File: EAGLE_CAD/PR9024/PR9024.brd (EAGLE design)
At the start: 70 x 70 mm, 75 parts, among them SW1 C&K_PTS645

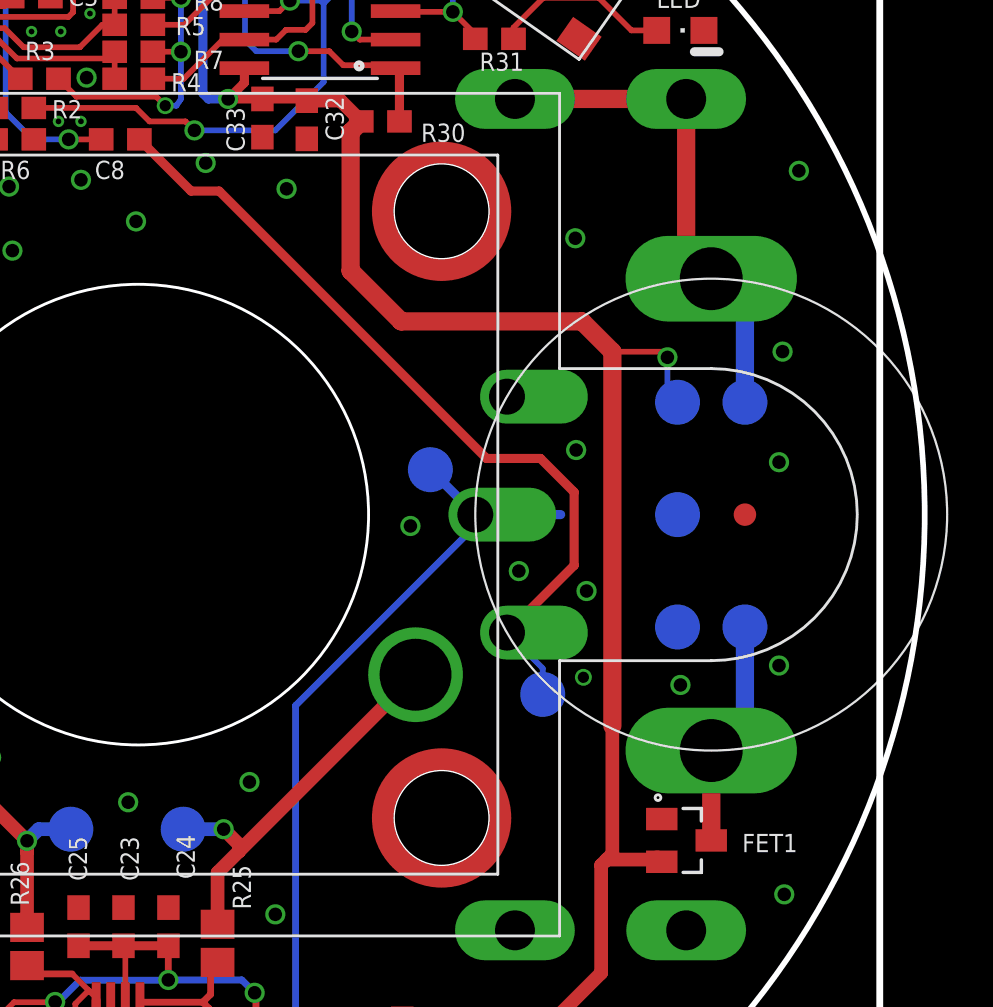
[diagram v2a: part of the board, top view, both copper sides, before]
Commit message: updated pot & rerouted stuff
new pot is Hong Yu Innovation Electronics Co
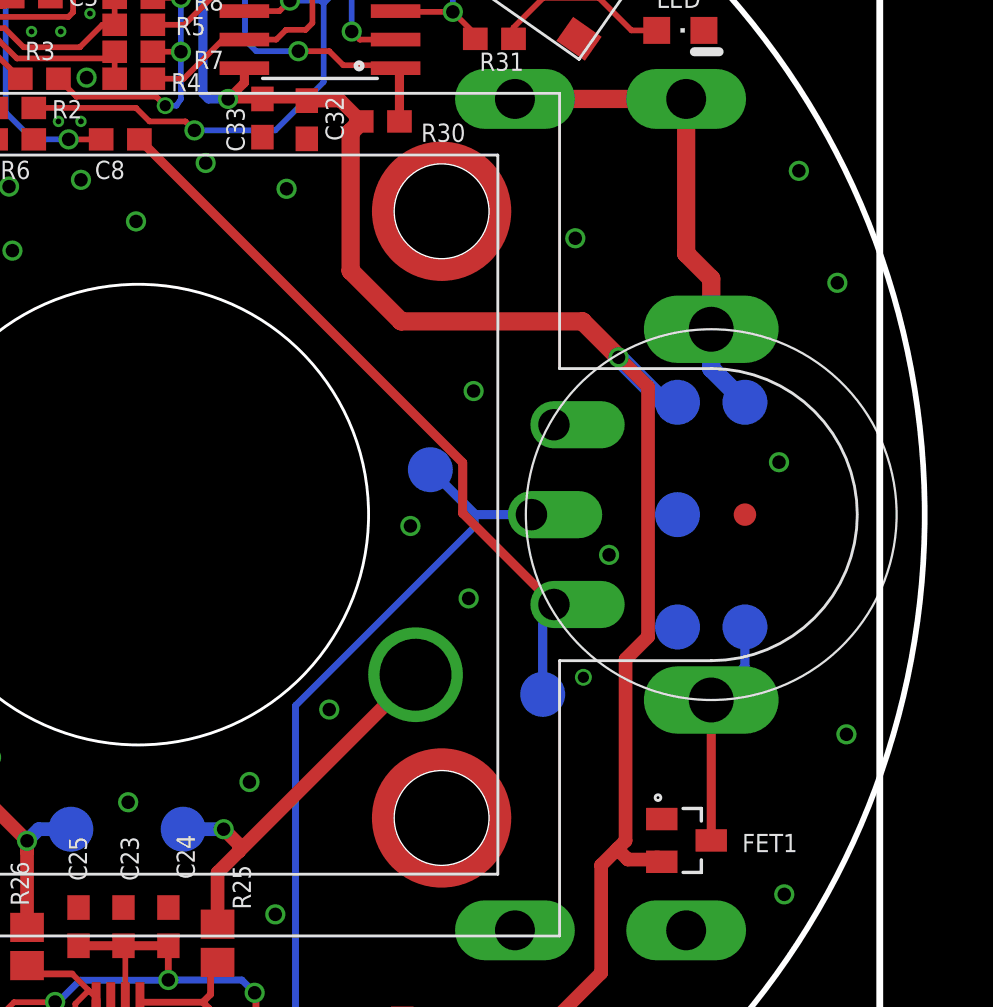
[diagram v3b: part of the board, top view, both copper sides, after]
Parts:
- R1: value (none) -> VOLUME_POT; device PR_Parts_Library:RV170SF_SW_POT -> PR_Parts_Library:H17112NS_A10K_L20F-002
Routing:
- net A_IN: track 36.8 -> 32.5 mm
- net A_OUT: track 35.7 -> 34.4 mm
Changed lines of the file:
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@@
 <?xml version="1.0" encoding="utf-8"?>
 <!DOCTYPE eagle SYSTEM "eagle.dtd">
-<eagle version="6.6.0">
+<eagle version="7.7.0">
 <drawing>
 <settings>
@@
 <rectangle x1="35.7111" y1="10.3543" x2="35.7873" y2="10.3797" layer="26" rot="R90"/>
 <rectangle x1="35.6857" y1="10.2781" x2="35.8635" y2="10.3035" layer="26" rot="R90"/>
-<text x="64" y="35" size="0.8128" layer="26" font="vector" ratio="22" rot="MR270" align="center">PR9024
+<text x="65.25" y="35" size="0.8128" layer="26" font="vector" ratio="22" rot="MR270" align="center">PR9024
 Born + tuned in Brooklyn
 http://thepublicrad.io</text>
@@
 <pass name="Default">
 <param name="RoutingGrid" value="50mil"/>
+<param name="AutoGrid" value="1"/>
+<param name="Efforts" value="0"/>
+<param name="TopRouterVariant" value="1"/>
 <param name="tpViaShape" value="round"/>
 <param name="PrefDir.1" value="|"/>
@@
 </element>
 <element name="ANT_MOUNT" library="PR_Parts_Library" package="PEM_M3" value="DNP" x="9.5" y="35" locked="yes" smashed="yes"/>
-<element name="R1" library="PR_Parts_Library" package="RV170SF_SW_POT" value="" x="60.5" y="35" locked="yes" rot="R270">
-<attribute name="MFG_PN" value="RV170SF-43-20F-A10K - supplied by CL Labs" x="60.5" y="35" size="1.778" layer="27" rot="R270" display="off"/>
-</element>
+<element name="R1" library="PR_Parts_Library" package="H17112NS_A10K_L20F-002" value="VOLUME_POT" x="60.5" y="35" locked="yes" rot="R270"/>
 <element name="MCU" library="PR_Parts_Library" package="8-SOIC" value="" x="43.075" y="56.775" smashed="yes" rot="R90">
 <attribute name="NAME" x="41.473" y="59.475" size="0.8128" layer="25" font="vector" ratio="16"/>
@@
 <via x="21.8" y="13.9" extent="1-16" drill="0.6"/>
 <via x="39.95" y="23.1" extent="1-16" drill="0.6"/>
-<via x="51.9375" y="32.4875" extent="1-16" drill="0.6"/>
 <via x="21.15375" y="64.95375" extent="1-16" drill="0.6"/>
 <contactref element="SW1" pad="P$1"/>
@@
 <via x="41.1" y="17.21" extent="1-16" drill="0.6"/>
 <via x="47.1125" y="34.495" extent="1-16" drill="0.6"/>
-<via x="54.4875" y="37.875" extent="1-16" drill="0.6"/>
-<via x="54.95" y="31.6" extent="1-16" drill="0.6"/>
+<via x="49.925" y="40.5" extent="1-16" drill="0.6"/>
 <via x="54.45" y="47.3" extent="1-16" drill="0.6"/>
 <via x="30.25" y="56.5" extent="1-16" drill="0.254"/>
@@
 <via x="33.36" y="59.265" extent="1-16" drill="0.5"/>
 <via x="54.81" y="27.76" extent="1-16" drill="0.5"/>
-<via x="59.13" y="27.42" extent="1-16" drill="0.6"/>
 <contactref element="LED" pad="C"/>
 <via x="44.2175" y="6.60875" extent="1-16" drill="0.6"/>
@@
 <via x="5.8675" y="51.235" extent="1-16" drill="0.6"/>
 <via x="23.7125" y="7.325" extent="1-16" drill="0.6"/>
-<via x="63.675" y="42.255" extent="1-16" drill="0.6"/>
-<via x="63.51625" y="28.285" extent="1-16" drill="0.6"/>
+<via x="66.1125" y="45.3175" extent="1-16" drill="0.6"/>
+<via x="66.51625" y="25.2225" extent="1-16" drill="0.6"/>
 <via x="63.51625" y="37.33375" extent="1-16" drill="0.6"/>
 <via x="51.59125" y="6.7675" extent="1-16" drill="0.6"/>
@@
 <vertex x="2" y="2"/>
 </polygon>
+<via x="55.95375" y="33.20875" extent="1-16" drill="0.6"/>
+<via x="49.70375" y="31.27125" extent="1-16" drill="0.6"/>
+<via x="43.5" y="26.325" extent="1-16" drill="0.6"/>
 </signal>
 <signal name="N$1">
@@
 <contactref element="T5" pad="TP"/>
 <contactref element="C32" pad="1"/>
-<wire x1="56.1" y1="25.6" x2="56.1" y2="42.25" width="0.8128" layer="1"/>
 <contactref element="FET1" pad="2"/>
 <wire x1="58.1" y1="19.65" x2="58.3" y2="19.55" width="0.8128" layer="1"/>
 <wire x1="55.6" y1="14.6" x2="55.6" y2="19.4" width="0.6096" layer="1"/>
-<wire x1="58.1" y1="19.65" x2="55.85" y2="19.65" width="0.6096" layer="1"/>
-<wire x1="55.85" y1="19.65" x2="55.6" y2="19.4" width="0.6096" layer="1"/>
-<wire x1="55.85" y1="19.65" x2="56.1" y2="19.9" width="0.6096" layer="1"/>
-<wire x1="56.1" y1="19.9" x2="56.1" y2="25.6" width="0.6096" layer="1"/>
-<wire x1="56.1" y1="42.25" x2="54.75" y2="43.6" width="0.8128" layer="1"/>
-<wire x1="54.75" y1="43.6" x2="46.7" y2="43.6" width="0.8128" layer="1"/>
+<wire x1="54.775" y1="43.6" x2="46.7" y2="43.6" width="0.8128" layer="1"/>
 <wire x1="46.7" y1="43.6" x2="44.45" y2="45.85" width="0.8128" layer="1"/>
-<wire x1="59" y1="40" x2="58.55" y2="40.45" width="0.254" layer="16"/>
-<wire x1="58.55" y1="40.45" x2="58.55" y2="42" width="0.254" layer="16"/>
-<via x="58.55" y="42" extent="1-16" drill="0.6"/>
-<wire x1="58.55" y1="42" x2="58.3" y2="42.25" width="0.254" layer="1"/>
-<wire x1="58.3" y1="42.25" x2="56.1" y2="42.25" width="0.254" layer="1"/>
 <wire x1="41.9375" y1="12.13" x2="46.43" y2="12.13" width="0.3048" layer="1"/>
 <wire x1="46.43" y1="12.13" x2="46.75" y2="11.81" width="0.3048" layer="1"/>
@@
 <wire x1="33.625" y1="62.125" x2="34.675" y2="62.125" width="0.254" layer="1"/>
 <wire x1="34.675" y1="62.125" x2="34.7" y2="62.15" width="0.254" layer="1"/>
+<wire x1="59" y1="40" x2="58.375" y2="40" width="0.8128" layer="16"/>
+<wire x1="58.375" y1="40" x2="56.375" y2="42" width="0.8128" layer="16"/>
+<via x="56.375" y="42" extent="1-16" drill="0.6"/>
+<wire x1="56.375" y1="42" x2="54.775" y2="43.6" width="0.8128" layer="1"/>
+<wire x1="55.6" y1="19.4" x2="56.31875" y2="20.11875" width="0.6096" layer="1"/>
+<wire x1="56.31875" y1="20.11875" x2="56.6875" y2="20.4875" width="0.6096" layer="1"/>
+<wire x1="56.6875" y1="20.4875" x2="56.6875" y2="28.5625" width="0.6096" layer="1"/>
+<wire x1="56.6875" y1="28.5625" x2="57.6875" y2="29.5625" width="0.6096" layer="1"/>
+<wire x1="57.6875" y1="29.5625" x2="57.6875" y2="40.6875" width="0.6096" layer="1"/>
+<wire x1="57.6875" y1="40.6875" x2="56.375" y2="42" width="0.6096" layer="1"/>
+<wire x1="58.1" y1="19.65" x2="56.7875" y2="19.65" width="0.6096" layer="1"/>
+<wire x1="56.7875" y1="19.65" x2="56.31875" y2="20.11875" width="0.6096" layer="1"/>
 </signal>
 <signal name="N$20">
@@
 <contactref element="T17" pad="TP"/>
 <contactref element="C22" pad="2"/>
-<wire x1="53.8" y1="35" x2="50" y2="35" width="0.4064" layer="16"/>
 <wire x1="48" y1="37" x2="50" y2="35" width="0.4064" layer="16"/>
 <wire x1="41.9375" y1="9.23" x2="41.9375" y2="10.4375" width="0.3048" layer="1"/>
@@
 <wire x1="42" y1="26.5" x2="50" y2="34.5" width="0.3048" layer="16"/>
 <wire x1="50" y1="34.5" x2="50" y2="35" width="0.3048" layer="16"/>
+<wire x1="52.5" y1="35" x2="50" y2="35" width="0.4064" layer="16"/>
 </signal>
 <signal name="N$23">
@@
 <contactref element="R1" pad="SW_IN"/>
 <contactref element="FET1" pad="3"/>
-<wire x1="60.5" y1="20.5" x2="60.5" y2="24.5" width="0.8128" layer="1"/>
 <contactref element="T14" pad="TP"/>
-<wire x1="60.5" y1="24.5" x2="62" y2="26" width="0.8128" layer="16"/>
-<wire x1="62" y1="26" x2="62" y2="30" width="0.8128" layer="16"/>
+<wire x1="60.5" y1="26.75" x2="62" y2="28.25" width="0.4064" layer="16"/>
+<wire x1="62" y1="28.25" x2="62" y2="30" width="0.4064" layer="16"/>
+<wire x1="60.5" y1="20.5" x2="60.5" y2="26.75" width="0.4064" layer="1"/>
 </signal>
 <signal name="A_IN">
 <contactref element="R1" pad="SIGNAL"/>
 <contactref element="C8" pad="2"/>
-<wire x1="51.41" y1="29.75" x2="54.4" y2="32.74" width="0.4064" layer="1"/>
-<wire x1="54.4" y1="32.74" x2="54.4" y2="36" width="0.4064" layer="1"/>
-<wire x1="54.4" y1="36" x2="52.9" y2="37.5" width="0.4064" layer="1"/>
-<wire x1="52.9" y1="37.5" x2="50.5" y2="37.5" width="0.4064" layer="1"/>
 <contactref element="T16" pad="TP"/>
-<wire x1="53" y1="27" x2="53" y2="28.16" width="0.254" layer="16"/>
-<wire x1="53" y1="28.16" x2="51.41" y2="29.75" width="0.254" layer="16"/>
-<wire x1="37.35" y1="49.4" x2="35.05" y2="51.7" width="0.4064" layer="1"/>
-<wire x1="50.5" y1="37.5" x2="38.6" y2="49.4" width="0.4064" layer="1"/>
-<wire x1="38.6" y1="49.4" x2="37.35" y2="49.4" width="0.4064" layer="1"/>
+<wire x1="35.05" y1="51.7" x2="49.4375" y2="37.3125" width="0.4064" layer="1"/>
+<wire x1="49.4375" y1="37.3125" x2="49.4375" y2="35.0625" width="0.4064" layer="1"/>
+<wire x1="49.4375" y1="35.0625" x2="53.5" y2="31" width="0.4064" layer="1"/>
+<wire x1="53" y1="27" x2="53" y2="30.5" width="0.4064" layer="16"/>
+<wire x1="53" y1="30.5" x2="53.5" y2="31" width="0.4064" layer="16"/>
 </signal>
 <signal name="RESET">
@@
 <wire x1="51.764" y1="53.5" x2="59.384" y2="53.5" width="0.8128" layer="1"/>
 <wire x1="59.384" y1="53.5" x2="59.384" y2="46.616" width="0.8128" layer="1"/>
+<contactref element="T15" pad="TP"/>
 <wire x1="59.384" y1="46.616" x2="60.5" y2="45.5" width="0.8128" layer="1"/>
-<contactref element="T15" pad="TP"/>
-<wire x1="60.5" y1="45.5" x2="62" y2="44" width="0.8128" layer="16"/>
-<wire x1="62" y1="44" x2="62" y2="40" width="0.8128" layer="16"/>
+<wire x1="60.5" y1="45.5" x2="60.5" y2="43.25" width="0.8128" layer="1"/>
+<wire x1="62" y1="40" x2="60.5" y2="41.5" width="0.8128" layer="16"/>
+<wire x1="60.5" y1="41.5" x2="60.5" y2="43.25" width="0.8128" layer="16"/>
 </signal>
 <signal name="ANT" class="1">
